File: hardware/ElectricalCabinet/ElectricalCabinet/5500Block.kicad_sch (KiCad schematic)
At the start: 0 parts

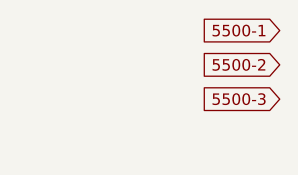
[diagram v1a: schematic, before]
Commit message: Further wiring updates
Populated 6100 Bus
Corrected number of relay boards
Added 110v outputs to relay boards and noted light positon
Uploaded light scheme to documents folder
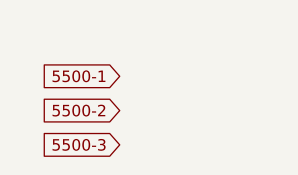
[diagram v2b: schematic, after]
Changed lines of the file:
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@@
 	(generator "eeschema")
 	(generator_version "10.0")
-	(paper "A4")
+	(paper "USLetter")
 	(global_label "5500-2"
 		(shape input)
-		(at 53.34 10.16 180)
+		(at 35.56 15.24 180)
 		(effects
 			(font
@@
 		)
 		(property "Intersheetrefs" "211"
-			(at 42.7349 10.16 0)
+			(at 24.9549 15.24 0)
 			(hide yes)
 			(show_name no)
@@
 		)
 		(property "Ref" "Ref 211"
-			(at 44.45 10.16 0)
+			(at 25.4 14.986 0)
 			(show_name no)
 			(do_not_autoplace no)
@@
 	(global_label "5500-3"
 		(shape input)
-		(at 53.34 13.97 180)
+		(at 35.56 19.05 180)
 		(effects
 			(font
@@
 		)
 		(property "Intersheetrefs" "${INTERSHEET_REFS}"
-			(at 42.7349 13.97 0)
+			(at 24.9549 19.05 0)
 			(hide yes)
 			(show_name no)
@@
 		)
 		(property "Ref" "Ref 2102"
-			(at 44.45 13.97 0)
+			(at 26.67 19.05 0)
 			(show_name no)
 			(do_not_autoplace no)
@@
 	(global_label "5500-1"
 		(shape input)
-		(at 53.34 6.35 180)
+		(at 35.56 11.43 180)
 		(effects
 			(font
@@
 		)
 		(property "Intersheetrefs" "107"
-			(at 42.7349 6.35 0)
+			(at 24.9549 11.43 0)
 			(hide yes)
 			(show_name no)
@@
 		)
 		(property "Ref" "Ref 107"
-			(at 44.704 6.35 0)
+			(at 25.4 11.43 0)
 			(show_name no)
 			(do_not_autoplace no)

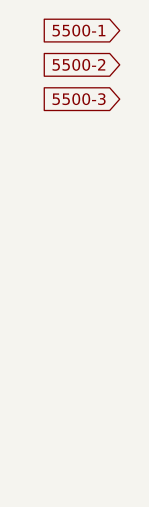
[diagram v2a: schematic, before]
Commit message: Schematic Update
Electrical Cabinet schematic done, this will be the last update unless something else needs to be changed.
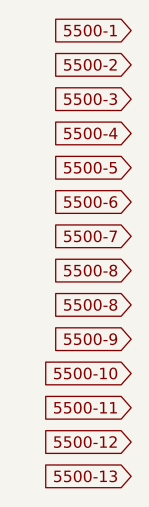
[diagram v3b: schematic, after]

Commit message: Electrical Cabinet done
Electrical Cabinet done, let me know if there are any changes or mistakes.
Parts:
- added U70, U71, U72, U73, U74, U75, U76: (no value), symbol TrafficLightLibrary:Terminal_Block
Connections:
- net 5500-1: now also U70. (2)
- net 5500-10: now also U73. (2)
- net 5500-11: now also U72. (2)
- net 5500-12: now also U71. (2)
- net 5500-13: now also U70. (2)
- net 5500-2: now also U71. (2)
- net 5500-3: now also U72. (2)
- net 5500-4: now also U73. (2)
- net 5500-5: now also U74. (2)
- net 5500-6: now also U75. (2)
- net 5500-7: now also U76. (2)
- net 5500-8: now also U75. (2), U76. (2)
- net 5500-9: now also U74. (2)
- new net: U70. (2), U71. (2), U72. (2), U73. (2), U74. (2), U75. (2), U76. (2)
